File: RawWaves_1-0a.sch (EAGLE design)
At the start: 53 parts, among them IC1 LM1117MP-5.0, IC4 TL074, U1 TEENSY_3.1_TW, X1 VERT_SD_CARD_REV2

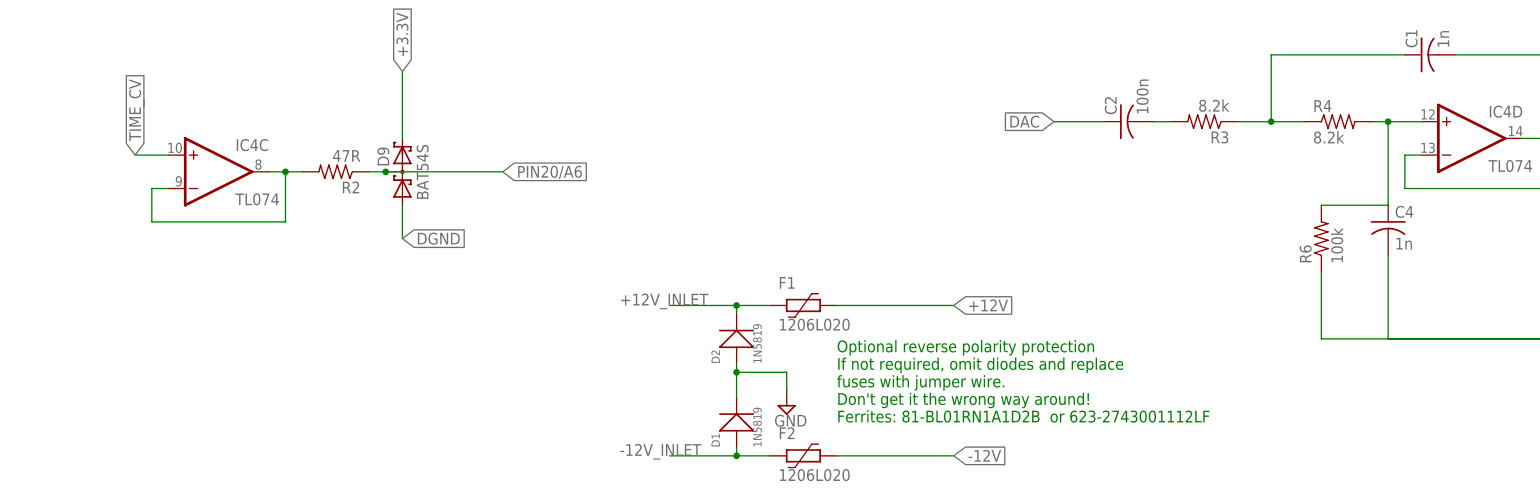
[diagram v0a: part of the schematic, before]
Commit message: Add Voltage Supervisor
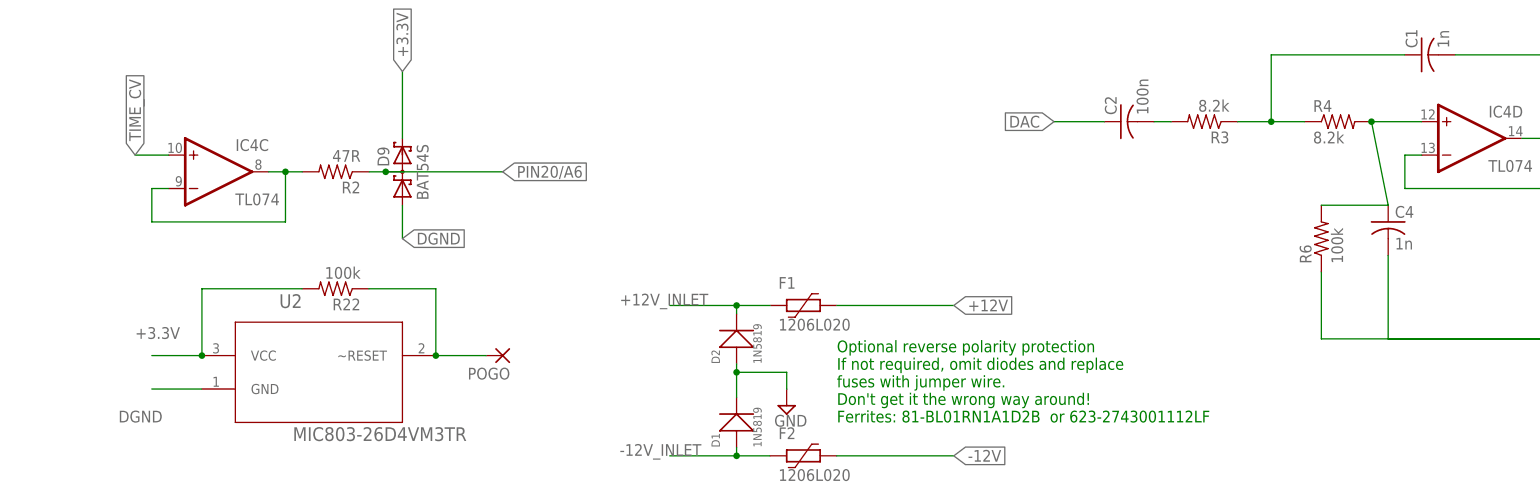
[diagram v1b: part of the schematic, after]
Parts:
- added POGO: (no value), wirepad:1,6/0,8
- added R22: 100k, rcl:R-US_R0805
- added U2: MIC803-26D4VM3TR, Micrel_By_element14_Batch_1:MIC803-26D4VM3TR
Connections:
- new net N$17: POGO.P, R22.1, U2.~RESET
- net +3.3V: now also R22.2, U2.VCC
- net DGND: now also U2.GND
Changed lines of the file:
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@@
 <part name="F1" library="polyfuse-smd_10" deviceset="?" device="1206L" technology="020"/>
 <part name="IC1" library="lm1117" deviceset="LM1117?-*" device="MP" technology="5.0"/>
+<part name="POGO" library="wirepad" library_urn="urn:adsk.eagle:library:412" deviceset="1,6/0,8" device="" package3d_urn="urn:adsk.eagle:package:30830/1"/>
+<part name="U2" library="Micrel_By_element14_Batch_1" deviceset="MIC803-26D4VM3TR" device=""/>
+<part name="R22" library="rcl" library_urn="urn:adsk.eagle:library:334" deviceset="R-US_" device="R0805" package3d_urn="urn:adsk.eagle:package:23553/2" value="100k"/>
 </parts>
 <sheets>
@@
 <attribute name="VALUE" x="287.02" y="12.7" size="1.778" layer="96"/>
 </instance>
+<instance part="POGO" gate="P" x="96.52" y="-71.12" smashed="yes" rot="R180">
+<attribute name="NAME" x="97.663" y="-72.9742" size="1.778" layer="95" rot="R180"/>
+<attribute name="VALUE" x="97.663" y="-67.818" size="1.778" layer="96" rot="R180"/>
+</instance>
+<instance part="U2" gate="A" x="50.8" y="-71.12" smashed="yes">
+<attribute name="NAME" x="62.5348" y="-63.881" size="2.0828" layer="95" ratio="10" rot="SR0"/>
+<attribute name="VALUE" x="64.5922" y="-84.0994" size="2.0828" layer="96" ratio="10" rot="SR0"/>
+</instance>
+<instance part="R22" gate="G$1" x="71.12" y="-60.96" smashed="yes" rot="R180">
+<attribute name="NAME" x="74.93" y="-62.4586" size="1.778" layer="95" rot="R180"/>
+<attribute name="VALUE" x="74.93" y="-57.658" size="1.778" layer="96" rot="R180"/>
+</instance>
 </instances>
 <busses>
@@
 <label x="147.32" y="127" size="1.016" layer="95" rot="R180" xref="yes"/>
 </segment>
+<segment>
+<pinref part="U2" gate="A" pin="VCC"/>
+<wire x1="50.8" y1="-71.12" x2="43.18" y2="-71.12" width="0.1524" layer="91"/>
+<label x="40.64" y="-68.58" size="1.778" layer="95"/>
+<pinref part="R22" gate="G$1" pin="2"/>
+<wire x1="66.04" y1="-60.96" x2="50.8" y2="-60.96" width="0.1524" layer="91"/>
+<wire x1="50.8" y1="-60.96" x2="50.8" y2="-71.12" width="0.1524" layer="91"/>
+<junction x="50.8" y="-71.12"/>
+</segment>
 </net>
 <net name="CHANNEL_CV" class="0">
@@
 <pinref part="D9" gate="G$1" pin="A1"/>
 <wire x1="81.28" y1="-48.26" x2="81.28" y2="-53.34" width="0.1524" layer="91"/>
+</segment>
+<segment>
+<pinref part="U2" gate="A" pin="GND"/>
+<wire x1="50.8" y1="-76.2" x2="43.18" y2="-76.2" width="0.1524" layer="91"/>
+<label x="38.1" y="-81.28" size="1.778" layer="95"/>
 </segment>
 </net>
@@
 <segment>
 <pinref part="R4" gate="G$1" pin="2"/>
-<wire x1="228.6" y1="-35.56" x2="231.14" y2="-35.56" width="0.1524" layer="91"/>
 <pinref part="C4" gate="G$1" pin="1"/>
-<wire x1="231.14" y1="-35.56" x2="236.22" y2="-35.56" width="0.1524" layer="91"/>
-<junction x="231.14" y="-35.56"/>
+<wire x1="228.6" y1="-35.56" x2="236.22" y2="-35.56" width="0.1524" layer="91"/>
+<junction x="228.6" y="-35.56"/>
 <pinref part="R6" gate="G$1" pin="2"/>
 <wire x1="220.98" y1="-48.26" x2="231.14" y2="-48.26" width="0.1524" layer="91"/>
-<wire x1="231.14" y1="-48.26" x2="231.14" y2="-35.56" width="0.1524" layer="91"/>
+<wire x1="231.14" y1="-48.26" x2="228.6" y2="-35.56" width="0.1524" layer="91"/>
 <pinref part="IC4" gate="D" pin="+IN"/>
 </segment>
@@
 </segment>
 </net>
+<net name="N$17" class="0">
+<segment>
+<pinref part="U2" gate="A" pin="~RESET"/>
+<pinref part="POGO" gate="P" pin="P"/>
+<wire x1="93.98" y1="-71.12" x2="86.36" y2="-71.12" width="0.1524" layer="91"/>
+<pinref part="R22" gate="G$1" pin="1"/>
+<wire x1="76.2" y1="-60.96" x2="86.36" y2="-60.96" width="0.1524" layer="91"/>
+<wire x1="86.36" y1="-60.96" x2="86.36" y2="-71.12" width="0.1524" layer="91"/>
+<junction x="86.36" y="-71.12"/>
+</segment>
+</net>
